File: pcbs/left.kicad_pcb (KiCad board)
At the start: 2 copper layers, 123.1 x 93.2 mm, 25 parts

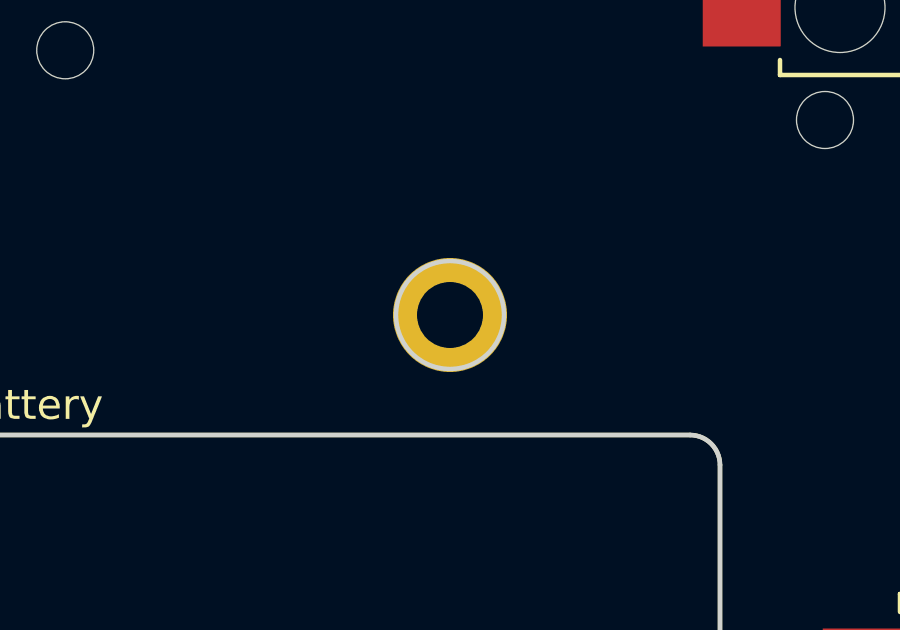
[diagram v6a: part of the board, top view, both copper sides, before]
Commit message: Remove bottom middle hole
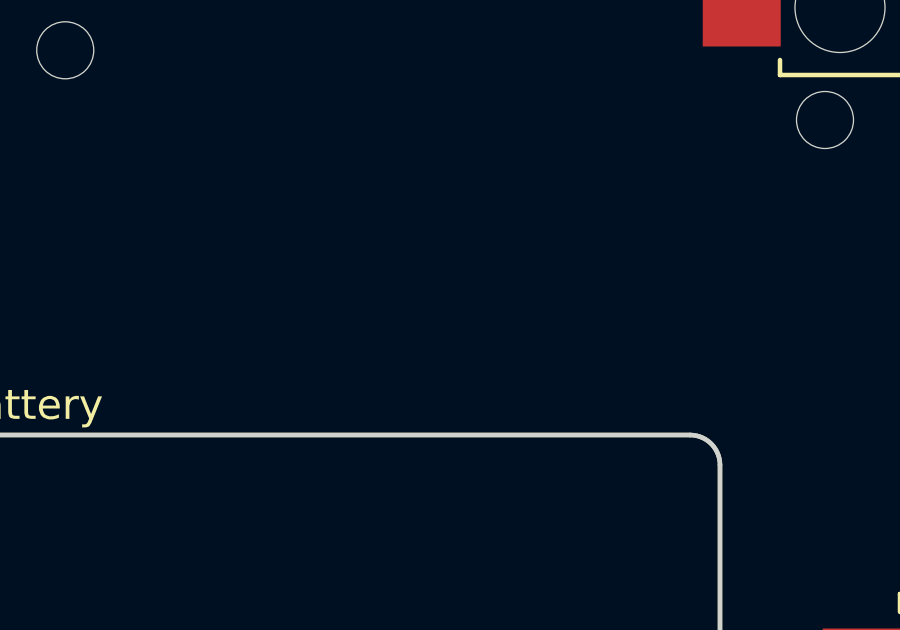
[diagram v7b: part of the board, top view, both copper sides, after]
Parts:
- removed H3: , ceoloide:mounting_hole_plated
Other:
- outline, holes or cut-outs redrawn
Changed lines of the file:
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@@
-    (fp_circle (center 0 0) (end -2.1500000000000004 0) (layer "B.CrtYd") (stroke (width 0.05) (type solid)) (fill none))
-  )
-  (footprint "ceoloide:mounting_hole_plated"
-    (layer "F.Cu")
-    (at 135.1483667 91.68429119999999 0)
-    (property "Reference" "H3"
-      (at 0 3 0)
-      (layer "F.SilkS")
-      hide
-      (effects (font (size 1 1) (thickness 0.15)))
-    )
-    (pad "" thru_hole circle (at 0 0 0) (size 3.8000000000000003 3.8000000000000003) (drill 2.2) (layers "*.Cu" "*.Mask"))
-    (fp_circle (center 0 0) (end -2.1500000000000004 0) (layer "F.CrtYd") (stroke (width 0.05) (type solid)) (fill none))
     (fp_circle (center 0 0) (end -2.1500000000000004 0) (layer "B.CrtYd") (stroke (width 0.05) (type solid)) (fill none))
   )
@@
 (gr_circle (center 94.25093449999999 45.301295800000005) (end 96.05093449999998 45.301295800000005) (layer Edge.Cuts) (stroke (width 0.15) (type default)) (fill none))
 (gr_circle (center 181.1483666 42.684291099999996) (end 182.9483666 42.684291099999996) (layer Edge.Cuts) (stroke (width 0.15) (type default)) (fill none))
-(gr_circle (center 135.1483667 91.68429119999999) (end 136.9483667 91.68429119999999) (layer Edge.Cuts) (stroke (width 0.15) (type default)) (fill none))
 (gr_line (start 112.1483666 96.68429119999999) (end 112.1483666 116.68429119999999) (layer F.SilkS) (stroke (width 0.15) (type default)))
 (gr_arc (start 112.1483666 116.68429119999999) (mid 112.4412598 117.391398) (end 113.1483666 117.68429119999999) (layer F.SilkS) (stroke (width 0.15) (type default)))
